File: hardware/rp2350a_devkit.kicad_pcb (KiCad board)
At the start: 2 copper layers, 29 x 60.5 mm, 55 parts, among them J1 USB_C_Receptacle_USB2.0_16P, J2 Conn_01x03, J3 Conn_01x16, J4 Conn_01x16, SW1 SW_Push, SW2 SW_Push, U1 NCP1117-3.3_SOT223, U2 USBLC6-2SC6, U3 W25Q128JVS, Y1 Crystal_GND24

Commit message: add images and files for v1.0a
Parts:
- removed SW1, SW2: SW_Push, Button_Switch_SMD:SW_SPST_B3U-1000P
- added BOOT: SW_Push, Button_Switch_SMD:SW_SPST_B3U-1000P, F.Cu at (157.0, 107.0)
- added D3: LED, LED_SMD:LED_0603_1608Metric, F.Cu at (160.2, 143.0)
- added RUN: SW_Push, Button_Switch_SMD:SW_SPST_B3U-1000P, F.Cu at (170.0, 140.5)
- C10, C11, C12, C13, C15, C16, C17, C18, C23, C4, C8: footprint Capacitor_SMD:C_0402_1005Metric -> Capacitor_SMD:C_0603_1608Metric
- C14: value 100n -> 10u; footprint Capacitor_SMD:C_0402_1005Metric -> Capacitor_SMD:C_0805_2012Metric
- C19: value 10u -> 100n
- C20: value 4.7u -> 100n; footprint Capacitor_SMD:C_0402_1005Metric -> Capacitor_SMD:C_0603_1608Metric
- C21, C22: value 4.7u -> 100n; footprint footprints:C_0402_smallpads -> Capacitor_SMD:C_0603_1608Metric
- C24, C9: footprint Capacitor_SMD:C_0603_1608Metric -> Capacitor_SMD:C_0805_2012Metric
- C3: value 100n -> 15p; footprint Capacitor_SMD:C_0402_1005Metric -> Capacitor_SMD:C_0603_1608Metric
- C5: value 15p -> 4.7u; footprint Capacitor_SMD:C_0402_1005Metric -> Capacitor_SMD:C_0603_1608Metric
- C6: value 100u -> 4.7u; footprint Capacitor_SMD:C_0402_1005Metric -> Capacitor_SMD:C_0603_1608Metric
- C7: value 100n -> 4.7u; footprint Capacitor_SMD:C_0402_1005Metric -> Capacitor_SMD:C_0603_1608Metric
- D1: value LED -> D_Schottky; footprint LED_SMD:LED_0402_1005Metric -> Diode_SMD:D_SOD-123
- D2: footprint LED_SMD:LED_0402_1005Metric -> LED_SMD:LED_0603_1608Metric
- J1: value USB_C_Receptacle_USB2.0_16P -> Conn_01x03; footprint Connector_USB:USB_C_Receptacle_G-Switch_GT-USB-7010ASV -> Connector_PinHeader_2.54mm:PinHeader_1x03_P2.54mm_Vertical
- J2: value Conn_01x03 -> USB_C_Receptacle_USB2.0_16P; footprint Connector_PinHeader_2.54mm:PinHeader_1x03_P2.54mm_Vertical -> Connector_USB:USB_C_Receptacle_G-Switch_GT-USB-7010ASV
- R1: footprint Resistor_SMD:R_0402_1005Metric -> Resistor_SMD:R_0603_1608Metric
- R10, R9: value 10k -> 27; footprint Resistor_SMD:R_0402_1005Metric -> Resistor_SMD:R_0603_1608Metric
- R11: value 1k -> 5k1; footprint Resistor_SMD:R_0402_1005Metric -> Resistor_SMD:R_0603_1608Metric
- R12: value 27 -> 5k1; footprint Resistor_SMD:R_0402_1005Metric -> Resistor_SMD:R_0603_1608Metric
- R13: value 27 -> 1k; footprint Resistor_SMD:R_0402_1005Metric -> Resistor_SMD:R_0603_1608Metric
- R2: value 5k1 -> 33; footprint Resistor_SMD:R_0402_1005Metric -> Resistor_SMD:R_0603_1608Metric
- R3: value 5k1 -> 1k; footprint Resistor_SMD:R_0402_1005Metric -> Resistor_SMD:R_0603_1608Metric
- R4, R6, R8: value 1k -> 10k; footprint Resistor_SMD:R_0402_1005Metric -> Resistor_SMD:R_0603_1608Metric
- R5: value 33 -> 10k; footprint Resistor_SMD:R_0402_1005Metric -> Resistor_SMD:R_0603_1608Metric
- R7: value 10k -> 1k; footprint Resistor_SMD:R_0402_1005Metric -> Resistor_SMD:R_0603_1608Metric
- U1: value NCP1117-3.3_SOT223 -> AP2112K-3.3; footprint Package_TO_SOT_SMD:SOT-223-3_TabPin2 -> Package_TO_SOT_SMD:SOT-23-5
- U2: value USBLC6-2SC6 -> RP2350A; footprint Package_TO_SOT_SMD:SOT-23-6 -> Package_DFN_QFN:QFN-60-1EP_7x7mm_P0.4mm_EP3.4x3.4mm
- U4: value ~ -> USBLC6-2SC6; footprint Package_DFN_QFN:QFN-60-1EP_7x7mm_P0.4mm_EP3.4x3.4mm -> Package_TO_SOT_SMD:SOT-23-6
- moved H2 76.1 mm to (178.5, 146.5)
- moved J1 65.2 mm to (165.5, 147.0), turned to 90 degrees
- moved R3 62.0 mm to (157.0, 146.5)
- moved R8 54.9 mm to (170.0, 137.0)
- moved R4 48.9 mm to (154.5, 138.5), turned to 0 degrees
- moved C3 47.2 mm to (155.5, 135.8), turned to -90 degrees
- moved C23 43.6 mm to (173.0, 123.8), turned to 0 degrees
- moved C24 42.2 mm to (173.8, 120.5)
- moved R13 42.0 mm to (160.2, 146.5), turned to -90 degrees
- moved H4 41.0 mm to (151.5, 98.5)
- moved U2 39.3 mm to (164.4, 128.3), turned to 0 degrees
- moved R2 37.5 mm to (170.2, 120.2)
- moved J2 36.9 mm to (165.0, 100.0), turned to 180 degrees
- moved R5 32.5 mm to (154.5, 141.0), turned to 0 degrees
- moved C19 30.7 mm to (162.0, 135.8), turned to -90 degrees
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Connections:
- C1 pad 1: VBUS -> /5VIN
- C10 pad 1: +3V3 -> VBUS
- C11 pad 1: +3V3 -> +1V1
- C12 pad 1: +3V3 -> +1V1
- C13 pad 1: +3V3 -> +1V1
- C14 pad 1: +3V3 -> +1V1
- C20 pad 1: /VREG_AVDD -> +3V3
- C22 pad 1: +1V1 -> +3V3
- C3 pad 1: VBUS -> /XIN
- C4 pad 1: /XIN -> /XTAL_OUT
- C5 pad 1: /XTAL_OUT -> /VREG_AVDD
- C6 pad 1: +1V1 -> +3V3
- C8 pad 1: +1V1 -> +3V3
- C9 pad 1: +1V1 -> +3V3
- D1 pad 1: Net-(D1-K) -> /5VIN
- D1 pad 2: +3V3 -> VBUS
- D2 pad 1: Net-(D2-K) -> /POWER_LED
- D2 pad 2: /IO15 -> +3V3
- J4 pad 1: GND -> VBUS
- J4 pad 16: unconnected-(J4-Pin_16-Pad16) -> GND
- R10 pad 1: /IO14/SDA -> /USB_R+
- R10 pad 2: +3V3 -> /USB_DOUT+
- R11 pad 1: /RUN_SW -> /CC1
- R11 pad 2: Net-(U4-RUN) -> GND
- R12 pad 1: /USB_R+ -> /CC2
- R12 pad 2: /USB_DOUT+ -> GND
- R13 pad 1: /USB_R- -> Net-(D3-K)
- R13 pad 2: /USB_DOUT- -> GND
- R2 pad 1: /CC1 -> +3V3
- R2 pad 2: GND -> /VREG_AVDD
- R3 pad 1: /CC2 -> /POWER_LED
- R4 pad 1: Net-(D1-K) -> /IO13/SCL
- R4 pad 2: GND -> +3V3
- R5 pad 1: +3V3 -> /IO14/SDA
- R5 pad 2: /VREG_AVDD -> +3V3
- R6 pad 1: Net-(D2-K) -> +3V3
- R6 pad 2: GND -> /QSPI_SS
- R7 pad 1: +3V3 -> /BOOT_SW
- R8 pad 1: /BOOT_SW -> /RUN_SW
- R8 pad 2: /QSPI_SS -> +3V3
- R9 pad 1: /IO13/SCL -> /USB_R-
- R9 pad 2: +3V3 -> /USB_DOUT-
- U1 pad 1: GND -> /5VIN
- U1 pad 2: +3V3 -> GND
- U1 pad 3: VBUS -> /5VIN
- U2 pad 1: /USB_DIN- -> +3V3
- U2 pad 2: GND -> /IO00
- U2 pad 3: /USB_DIN+ -> /IO01
- U2 pad 4: /USB_DOUT+ -> /IO02
- U2 pad 5: VBUS -> /IO03
- U2 pad 6: /USB_DOUT- -> +1V1
- U4 pad 1: +3V3 -> /USB_DIN-
- U4 pad 2: /IO00 -> GND
- U4 pad 3: /IO01 -> /USB_DIN+
- U4 pad 4: /IO02 -> /USB_DOUT+
- U4 pad 5: /IO03 -> VBUS
- U4 pad 6: +1V1 -> /USB_DOUT-
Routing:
- net +3V3: track 87.4 -> 115.3 mm, vias 5 -> 14
- net VBUS: track 14.9 -> 28.9 mm
- net /IO07: track 8.83 -> 22.0 mm, vias 0 -> 2
- net /IO06: track 9.96 -> 20.7 mm, vias 0 -> 1
- net /IO02: track 17.3 -> 27.3 mm, vias 0 -> 2
- net /RUN_SW: track 1.71 -> 11.2 mm, vias 0 -> 2
- net /IO08: track 8.61 -> 16.9 mm
- net Net-(U4-RUN): track 8.18 -> 0.00 mm
- net /IO04: track 14.0 -> 21.8 mm
- net /IO01: track 19.4 -> 27.1 mm
- net /IO05: track 11.9 -> 19.5 mm, vias 0 -> 1
- net /IO22: track 11.4 -> 18.9 mm
- net /IO09: track 9.37 -> 16.8 mm
- net /IO24: track 15.3 -> 22.3 mm
- net /QSPI_SD2: track 13.2 -> 6.21 mm, vias 2 -> 0
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- added copper zone on F.Cu, net /5VIN
- removed copper zone on F.Cu, net VBUS
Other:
- board size 29 x 60.5 mm -> 32 x 53 mm
- board text added: "3V3"
- board text added: "5V"
- board text added: "IOA0"
- board text added: "IOA1"
- board text added: "IOA2"
- board text added: "IOA3"
- board text added: "SWCLK"
- board text added: "SWDIO"
- board text removed: "+3V3"
- board text removed: "A0"
- board text removed: "A1"
- board text removed: "A2"
- board text removed: "A3"
- board text removed: "NC"

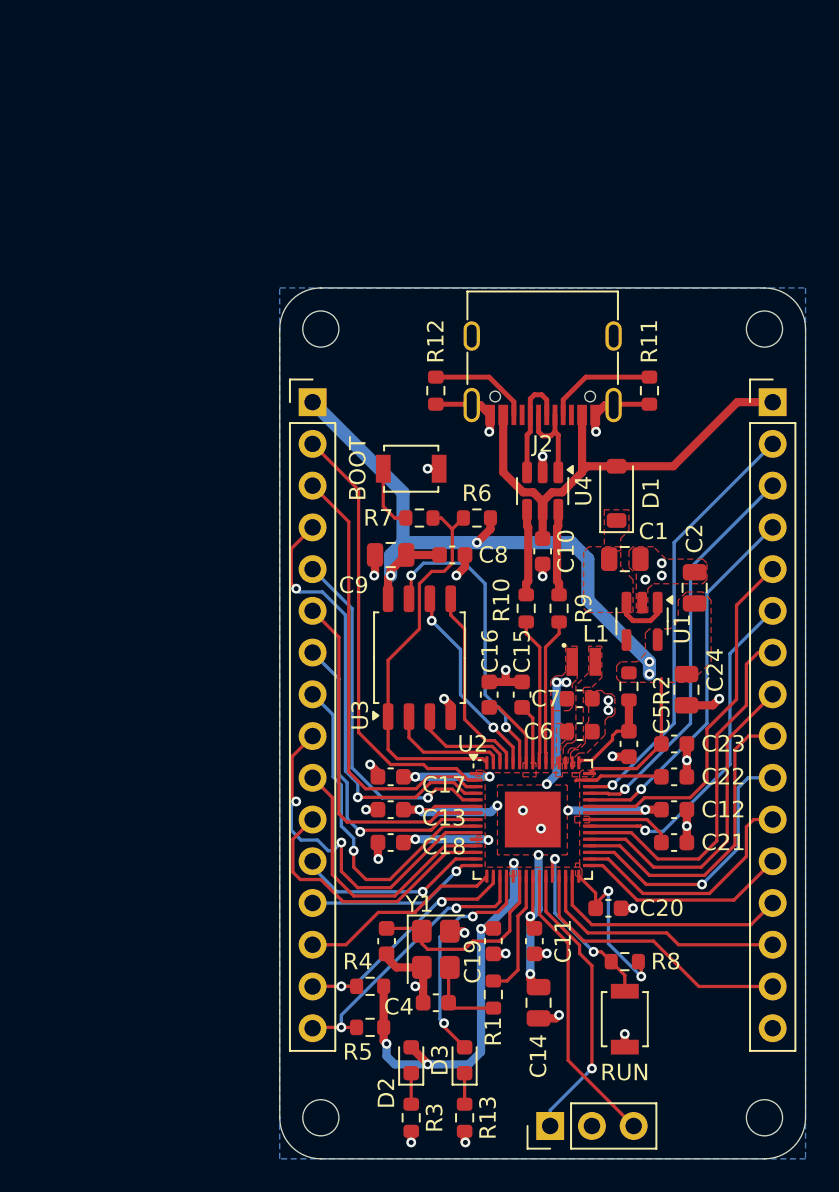
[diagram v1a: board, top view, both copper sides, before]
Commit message: re-routed pcb for a better ground plane
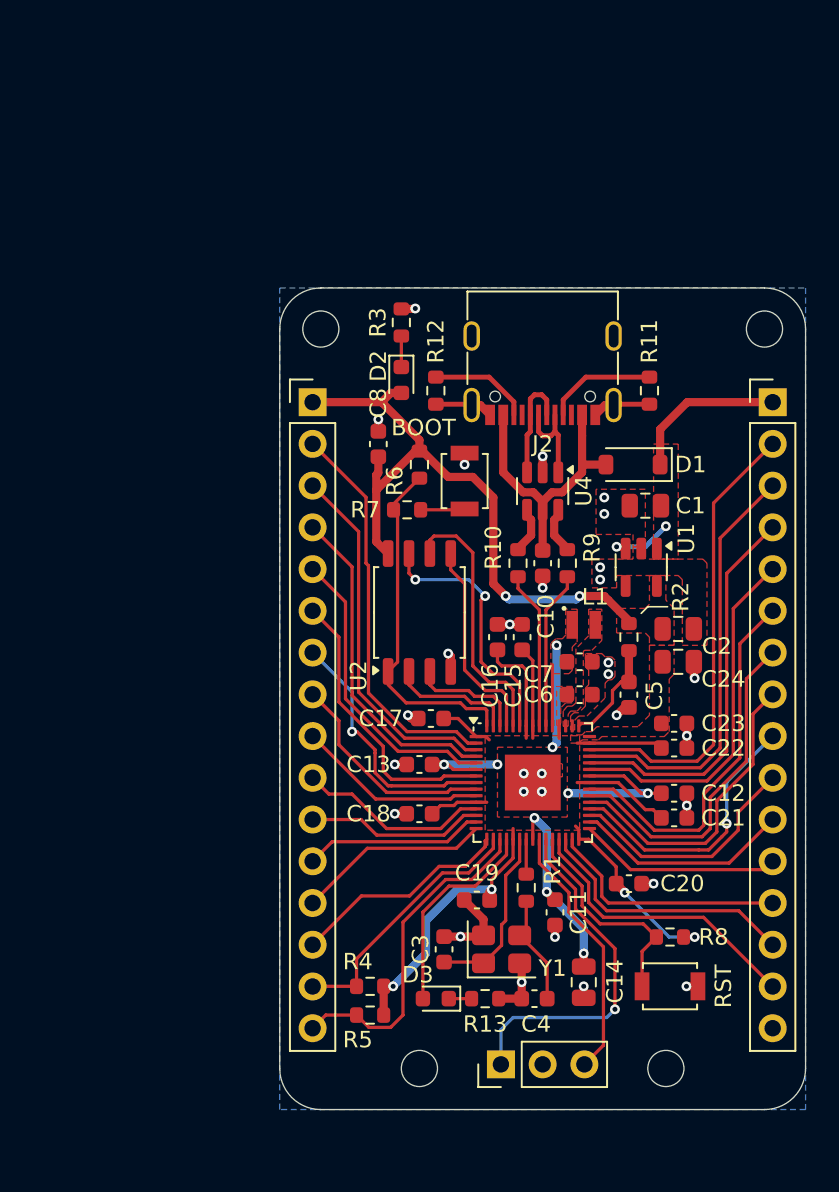
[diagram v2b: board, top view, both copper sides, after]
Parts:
- removed C9: 10u, Capacitor_SMD:C_0805_2012Metric
- moved R3 48.4 mm to (156.4, 98.1), turned to 90 degrees
- moved D2 41.4 mm to (156.4, 101.6), turned to -90 degrees
- moved C8 8.11 mm to (155.0, 105.5), turned to 90 degrees
- moved R13 7.36 mm to (161.5, 139.2), turned to 0 degrees
- moved R1 6.80 mm to (164.0, 132.5)
- moved H2 6.71 mm to (172.5, 143.5)
- moved H3 6.71 mm to (157.5, 143.5)
- moved C4 6.01 mm to (164.5, 139.2)
- moved J1 4.80 mm to (162.5, 143.2)
- moved R6 4.78 mm to (157.5, 106.8), turned to -90 degrees
- moved C17 4.31 mm to (158.2, 122.2)
- moved D3 4.14 mm to (158.5, 139.2), turned to 180 degrees
- moved Y1 4.00 mm to (162.5, 136.2), turned to 0 degrees
- moved C16 3.54 mm to (162.2, 117.2)
- moved C3 3.54 mm to (159.0, 136.2), turned to 90 degrees
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- renumbered RUN to RST
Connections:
- J4 pad 1: VBUS -> /5VIN
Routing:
- net +3V3: track 115.3 -> 99.9 mm, vias 14 -> 6
- net VBUS: track 28.9 -> 17.7 mm
- net /IO07: track 22.0 -> 11.6 mm, vias 2 -> 0
- net /5VIN: track 3.61 -> 13.8 mm, vias 0 -> 2
- net GND: track 40.4 -> 32.7 mm, vias 32 -> 30
- net /IO06: track 20.7 -> 13.4 mm, vias 1 -> 0
- net /IO02: track 27.3 -> 20.3 mm, vias 2 -> 0
- net /IO09: track 16.8 -> 10.8 mm
- net /XOUT: track 7.69 -> 2.12 mm
- net /IO08: track 16.9 -> 11.7 mm
- net /IO01: track 27.1 -> 22.3 mm
- net /IO04: track 21.8 -> 17.5 mm
- net /SWD: track 17.4 -> 21.7 mm
- net +1V1: track 41.9 -> 37.8 mm, vias 10 -> 9
- net /QSPI_SCLK: track 12.1 -> 16.1 mm, vias 2 -> 0
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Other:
- board size 32 x 53 mm -> 32 x 50 mm

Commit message: update 3d pcb image, fix silkscreen placement and resistor values
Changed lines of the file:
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@@
 		(tags "QFN NoLead")
 		(property "Reference" "U2"
-			(at -10.6 -6.5 90)
+			(at -4.15 -4.85 180)
 			(layer "F.SilkS")
 			(effects
@@
 			(at -3.5 -3.6 90)
 			(layer "F.SilkS")
-			(hide yes)
 			(effects
 				(font
@@
 		)
 		(property "Value" "W25Q128JVS"
-			(at 0 -3.75 90)
+			(at 0 3.6 90)
 			(layer "F.Fab")
 			(effects
@@
 			)
 		)
-		(property "Datasheet" "https://www.winbond.com/resource-files/w25q128jv_dtr%20revc%2003272018%20plus.pdf"
+		(property "Datasheet" ""
 			(at 0 0 90)
 			(layer "F.Fab")
@@
 			)
 		)
-		(property "Description" "128Mbit / 16MiB Serial Flash Memory, Standard/Dual/Quad SPI, 2.7-3.6V, SOIC-8"
+		(property "Description" ""
 			(at 0 0 90)
 			(layer "F.Fab")

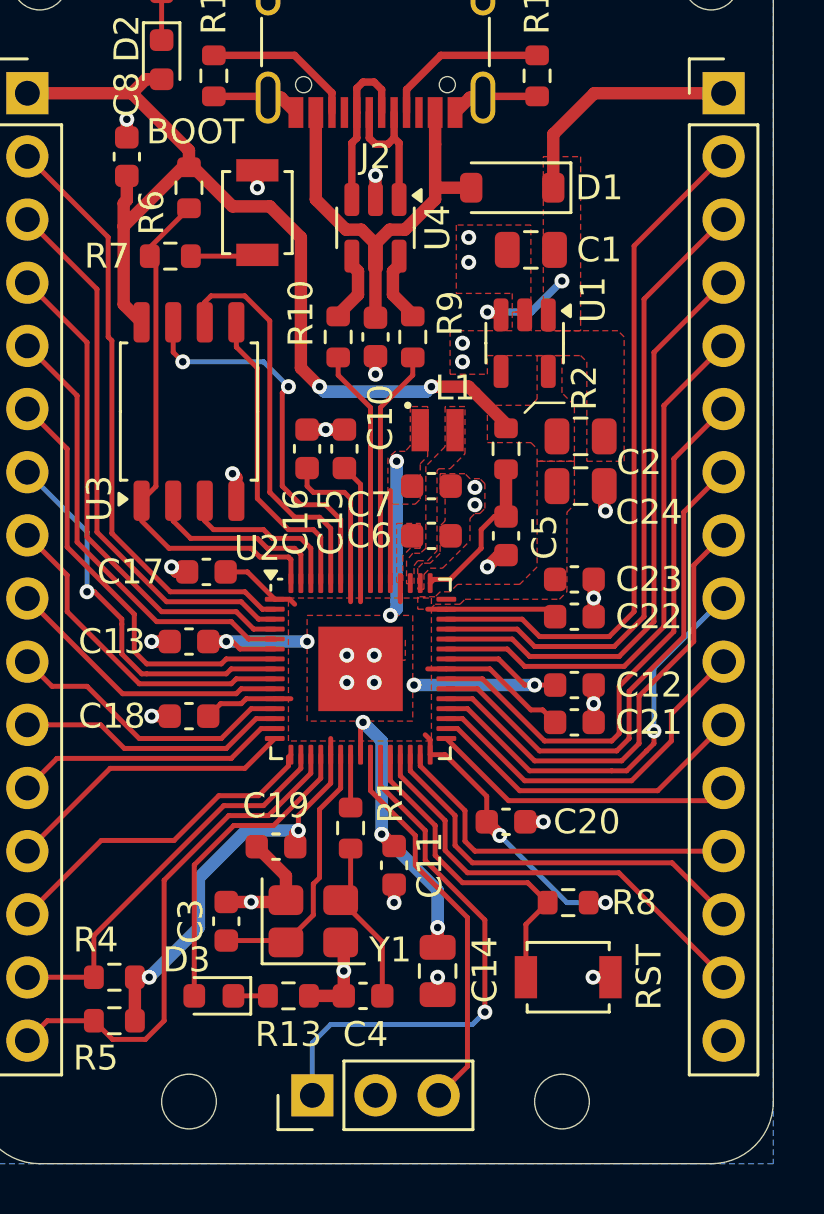
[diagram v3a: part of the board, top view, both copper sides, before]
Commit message: changed button footprint
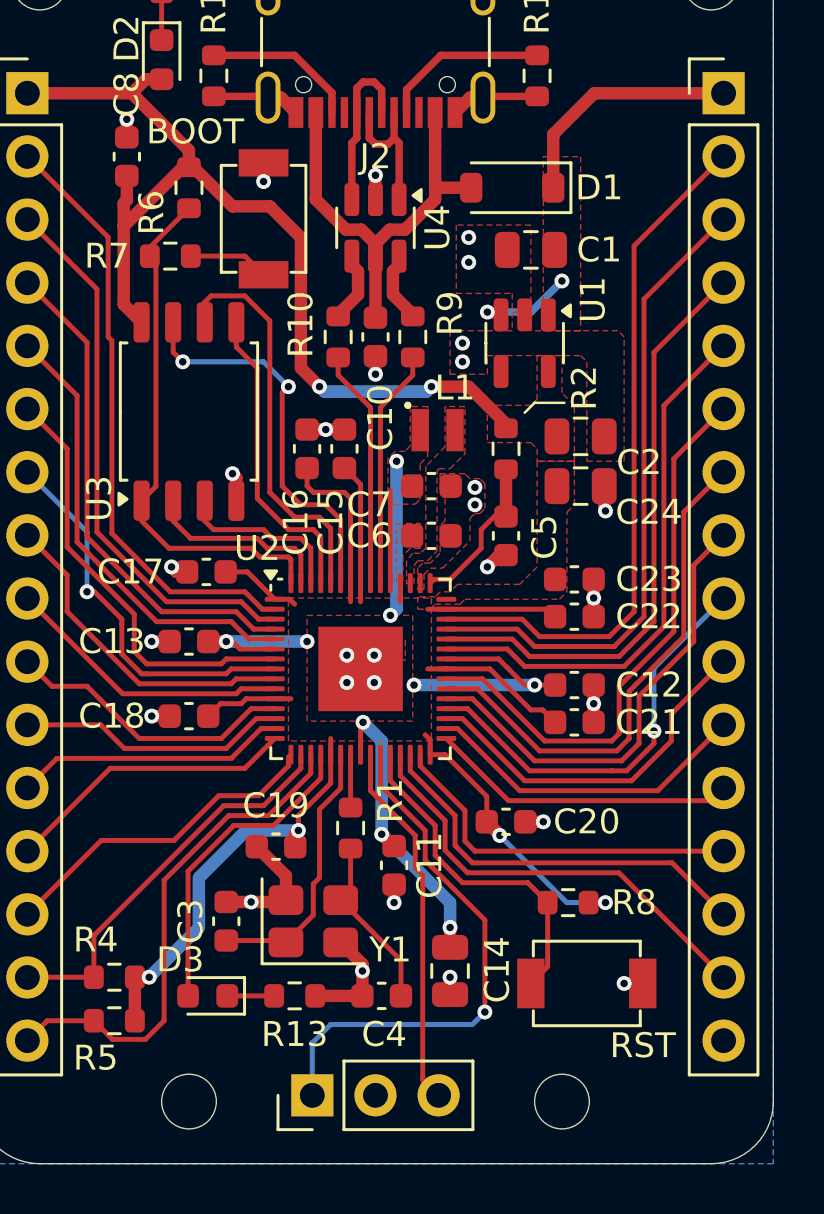
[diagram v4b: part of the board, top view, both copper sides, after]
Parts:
- BOOT, RST: footprint Button_Switch_SMD:SW_SPST_B3U-1000P -> footprints:TS-1088-AR02016
- R13, R3: value 1k -> 10k
- moved RST 0.79 mm to (173.5, 138.8)
- moved C4 0.75 mm to (165.2, 139.2)
- moved C14 0.50 mm to (168.0, 138.2)
- moved BOOT 0.35 mm to (160.5, 108.0)
- moved D3 0.25 mm to (158.2, 139.2)
- moved R13 0.25 mm to (161.8, 139.2)
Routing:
- net /SWCLK: track 15.8 -> 14.8 mm
- net GND: track 32.7 -> 33.6 mm
- net /BOOT_SW: track 2.70 -> 3.24 mm
- net Net-(D3-K): track 1.39 -> 1.89 mm
